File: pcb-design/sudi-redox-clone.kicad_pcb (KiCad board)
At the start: 2 copper layers, 123.4 x 99.4 mm, 151 parts, among them J1 SIDE_CON, J2 SWD_JLINK, J3 0.91 OLED, J4 BatCon, J5 SIDE_CON, K1 KEYSW, K10 KEYSW, K11 KEYSW, K12 KEYSW, K13 KEYSW, K14 KEYSW, K15 KEYSW, K16 KEYSW, K17 KEYSW, K18 KEYSW, K2 KEYSW, K3 KEYSW, K4 KEYSW, K5 KEYSW, K6 KEYSW, K7 KEYSW, K8 KEYSW, K9 KEYSW, P1 USB_C_Plug_USB2.0, Q1 PJA3404_(G1,D3,S2), Q2 PJA3405_(G1,D3,S2), SW1 RST, SW3 PWR_SWITCH, SW4 5V_EN, U4 CH340C, U5 BQ24075RGT_DPPM, U6 TPS63002_SEPIC_5V, U7 nRF52832-QFxx, U8 MCP23017_SS, U9 TPS63001_SEPIC_3V3, Y1 32MHz_CF4032M00020001

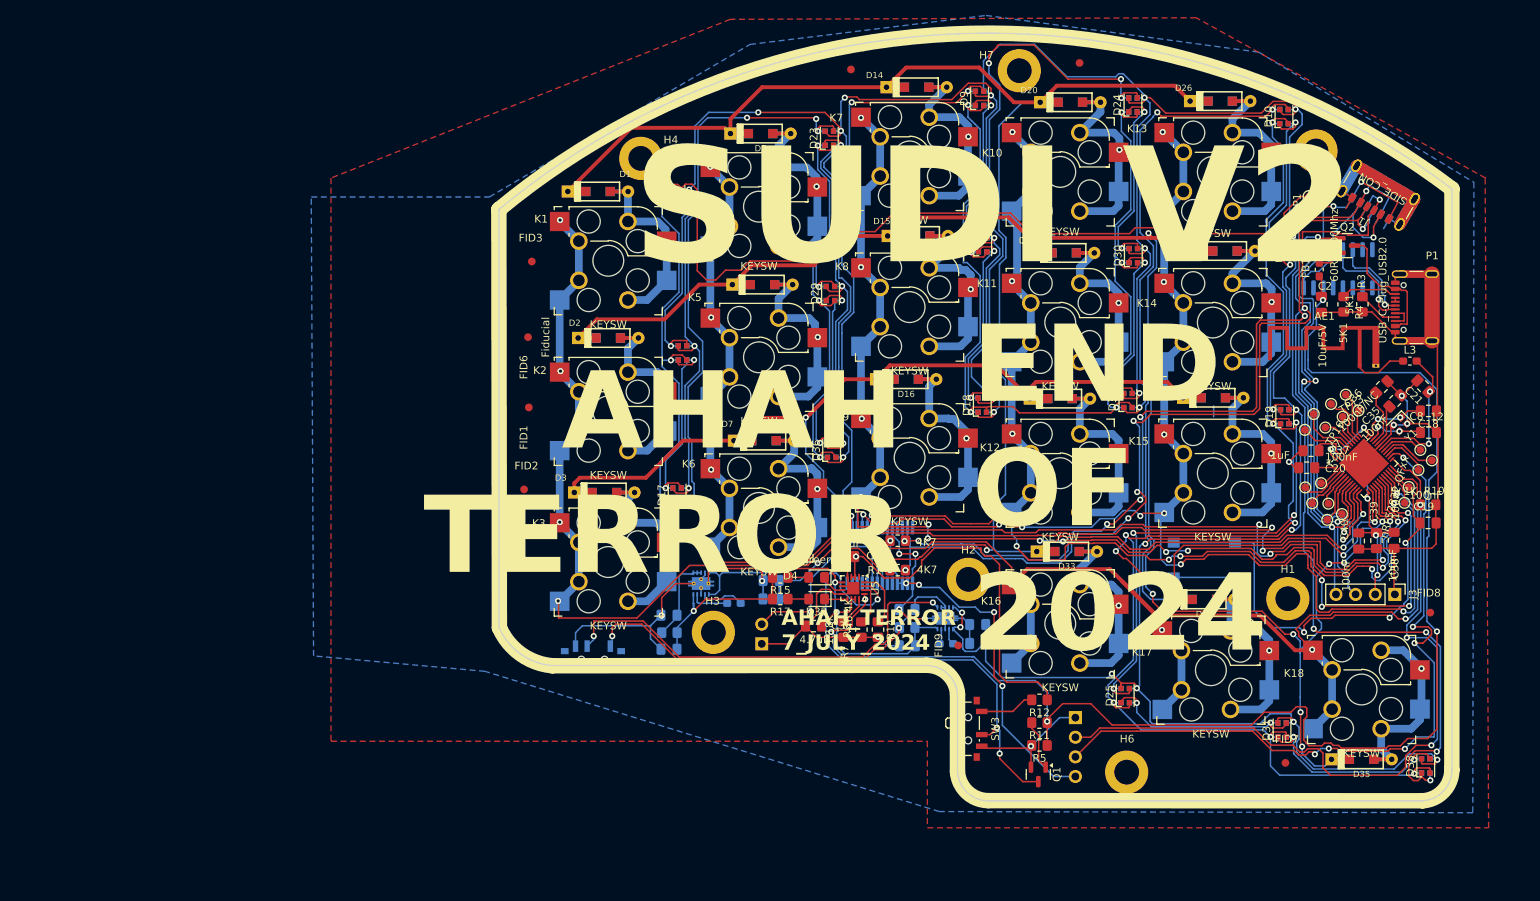
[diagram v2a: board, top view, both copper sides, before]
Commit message: [16-11-1807] add capacitor to WS2812C-2020
change gif
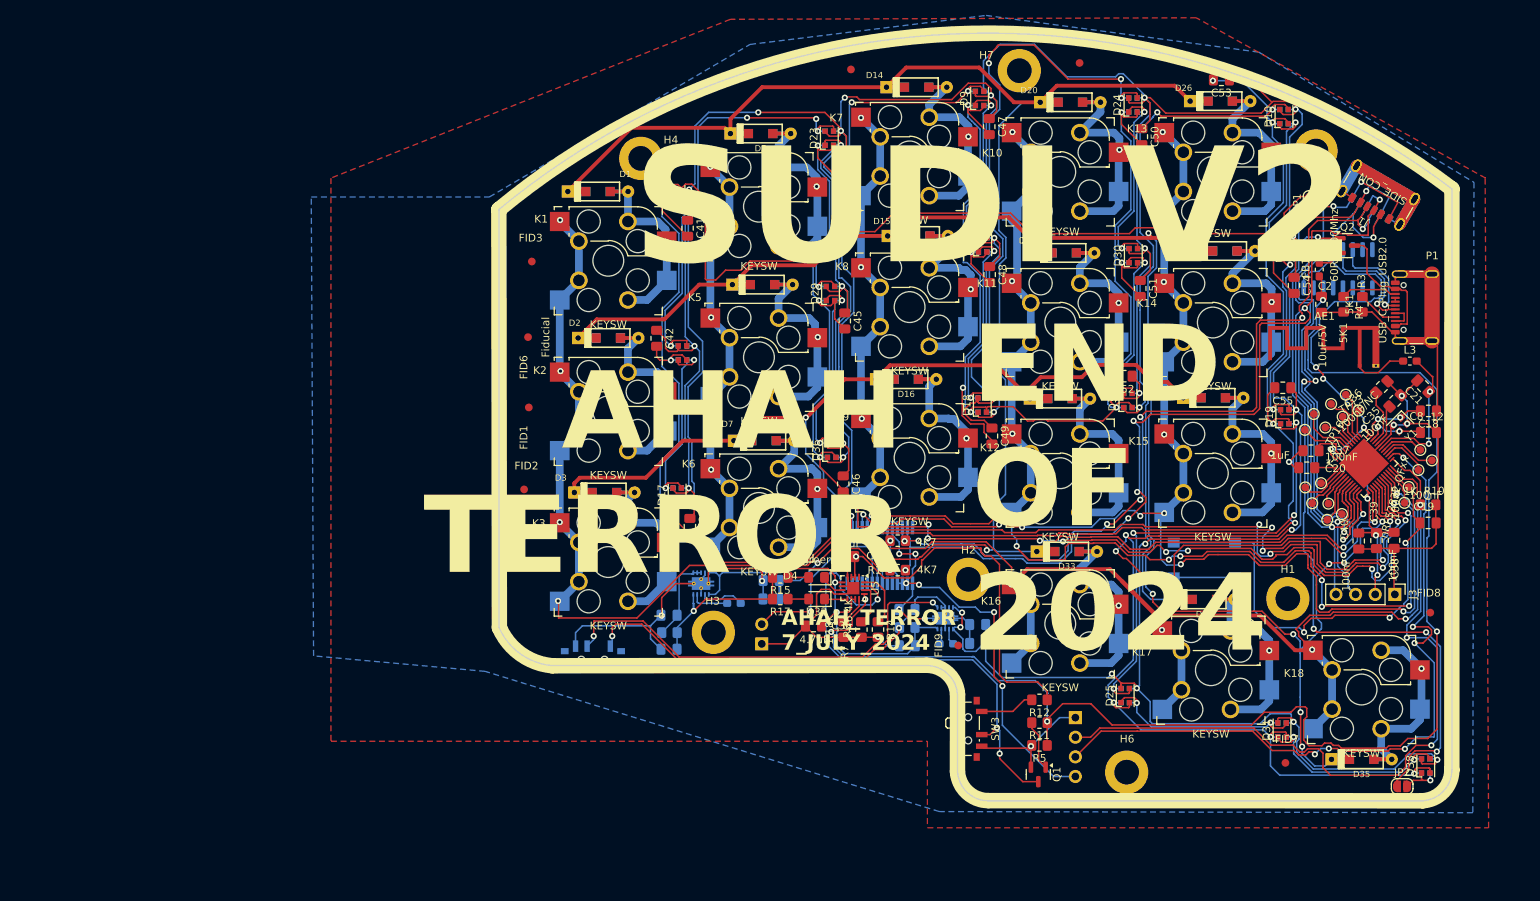
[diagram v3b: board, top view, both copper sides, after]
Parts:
- added C41: 100nF, Capacitor_SMD:C_0805_2012Metric_Pad1.18x1.45mm_HandSolder, F.Cu at (132.8, 70.9)
- added C42: 100nF, Capacitor_SMD:C_0805_2012Metric_Pad1.18x1.45mm_HandSolder, F.Cu at (128.8, 85.2)
- added C43: 100nF, Capacitor_SMD:C_0805_2012Metric_Pad1.18x1.45mm_HandSolder, F.Cu at (133.2, 109.5)
- added C44: 100nF, Capacitor_SMD:C_0805_2012Metric_Pad1.18x1.45mm_HandSolder, F.Cu at (152.6, 63.2)
- added C45: 100nF, Capacitor_SMD:C_0805_2012Metric_Pad1.18x1.45mm_HandSolder, F.Cu at (153.2, 82.9)
- added C46: 100nF, Capacitor_SMD:C_0805_2012Metric_Pad1.18x1.45mm_HandSolder, F.Cu at (153.0, 104.0)
- added C47: 100nF, Capacitor_SMD:C_0805_2012Metric_Pad1.18x1.45mm_HandSolder, F.Cu at (171.9, 57.8)
- added C48: 100nF, Capacitor_SMD:C_0805_2012Metric_Pad1.18x1.45mm_HandSolder, F.Cu at (171.9, 76.9)
- added C49: 100nF, Capacitor_SMD:C_0805_2012Metric_Pad1.18x1.45mm_HandSolder, F.Cu at (172.2, 97.8)
- added C50: 100nF, Capacitor_SMD:C_0805_2012Metric_Pad1.18x1.45mm_HandSolder, F.Cu at (191.7, 59.0)
- added C51: 100nF, Capacitor_SMD:C_0805_2012Metric_Pad1.18x1.45mm_HandSolder, F.Cu at (191.4, 78.7)
- added C52: 100nF, Capacitor_SMD:C_0805_2012Metric_Pad1.18x1.45mm_HandSolder, F.Cu at (189.3, 90.0)
- added C53: 100nF, Capacitor_SMD:C_0805_2012Metric_Pad1.18x1.45mm_HandSolder, F.Cu at (201.9, 51.7)
- added C54: 100nF, Capacitor_SMD:C_0805_2012Metric_Pad1.18x1.45mm_HandSolder, F.Cu at (211.3, 78.3)
- added C55: 100nF, Capacitor_SMD:C_0805_2012Metric_Pad1.18x1.45mm_HandSolder, F.Cu at (209.9, 91.5)
- added JP2: END_TX, Jumper:SolderJumper-2_P1.3mm_Open_RoundedPad1.0x1.5mm, F.Cu at (225.3, 143.2)
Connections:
- D38 pad 1: END_TX -> Net-(D38-DOUT)
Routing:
- net GND: track 699.1 -> 784.3 mm, vias 35 -> 37
- net +5V: track 558.7 -> 630.0 mm
- net +3.3V: track 140.8 -> 178.5 mm, vias 13 -> 15
- net Net-(D38-DOUT): track 0.00 -> 5.31 mm, vias 0 -> 1
- net END_TX: track 116.9 -> 113.9 mm, vias 7 -> 6
- net SDA: track 167.2 -> 164.9 mm
- net SCL: track 156.3 -> 154.4 mm
- net row3: track 218.0 -> 219.8 mm
- net Net-(P1-D+): track 13.3 -> 14.7 mm
- net Net-(P1-D-): track 11.3 -> 12.5 mm

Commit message: [17-11-1825] tweak values and silkscreen
nit, add pdf

nit

nit schematic

add svg
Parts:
- added C56: 0.1uF, Capacitor_SMD:C_0805_2012Metric_Pad1.18x1.45mm_HandSolder, B.Cu at (171.3, 106.4)
- added U10: MAX17048, Package_DFN_QFN:DFN-8-1EP_2x2mm_P0.5mm_EP0.8x1.6mm, B.Cu at (169.1, 109.6)
- SW4: moved to F.Cu
- TP1: value TestPoint -> 0
- TP10: value TestPoint -> 23
- TP11: value TestPoint -> 24
- TP12: value TestPoint -> 25
- TP13: value TestPoint -> 26
- TP14: value TestPoint -> 27
- TP15: value TestPoint -> 28
- TP16: value TestPoint -> 29
- TP17: value TestPoint -> 30
- TP18: value TestPoint -> 31
- TP2: value TestPoint -> 1
- TP3: value TestPoint -> 2
- TP4: value TestPoint -> 3
- TP5: value TestPoint -> 4
- TP6: value TestPoint -> 5
- TP7: value TestPoint -> 19
- TP8: value TestPoint -> 20
- TP9: value TestPoint -> 22
- moved SW4 1.08 mm to (120.7, 125.3), turned to 0 degrees
- moved SW3 0.60 mm to (170.1, 135.7)
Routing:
- net +3.3V: track 178.5 -> 251.9 mm, vias 15 -> 18
- net SDA: track 164.9 -> 173.1 mm
- net SCL: track 154.4 -> 159.0 mm
- net (no net): track 3.75 -> 0.00 mm
- net row1: track 231.4 -> 234.8 mm
- net +BATT: track 67.2 -> 70.6 mm
- net GND: track 784.3 -> 787.6 mm, vias 37 -> 38
- net Net-(SW4-A): track 53.6 -> 56.4 mm, vias 2 -> 3
- net Net-(SW4-B): track 56.0 -> 53.5 mm, vias 2 -> 1
- net col6: track 154.5 -> 156.0 mm
- net VBUS: track 183.0 -> 184.4 mm
- net /SWDIO: track 95.6 -> 94.7 mm
- net /SWCLK: track 96.3 -> 95.5 mm
- net row3: track 219.8 -> 220.6 mm
- net Net-(SW3-A): track 7.09 -> 6.49 mm
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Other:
- board text added: "FINISHED AT 17 NOV 2024"
- board text added: "VERSION 9 11 2023 17 11 2024"
- board text removed: "9 11 2023 7 7 2024 1 11 2024"
- board text removed: "FINISHED AT 16 NOV 2024"
